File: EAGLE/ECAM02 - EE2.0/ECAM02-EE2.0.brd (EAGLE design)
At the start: 82.6 x 75.9 mm, 54 parts, among them J1 MODULAR TOOL, J2 SPI, J3 MOT, J4 FTDI, J5 S4B-PH-SM4, J6 S5B-PH-SM, J7 RINGLIGHT, Q2 16MHz, U1 SP3485, U10 MCP4725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

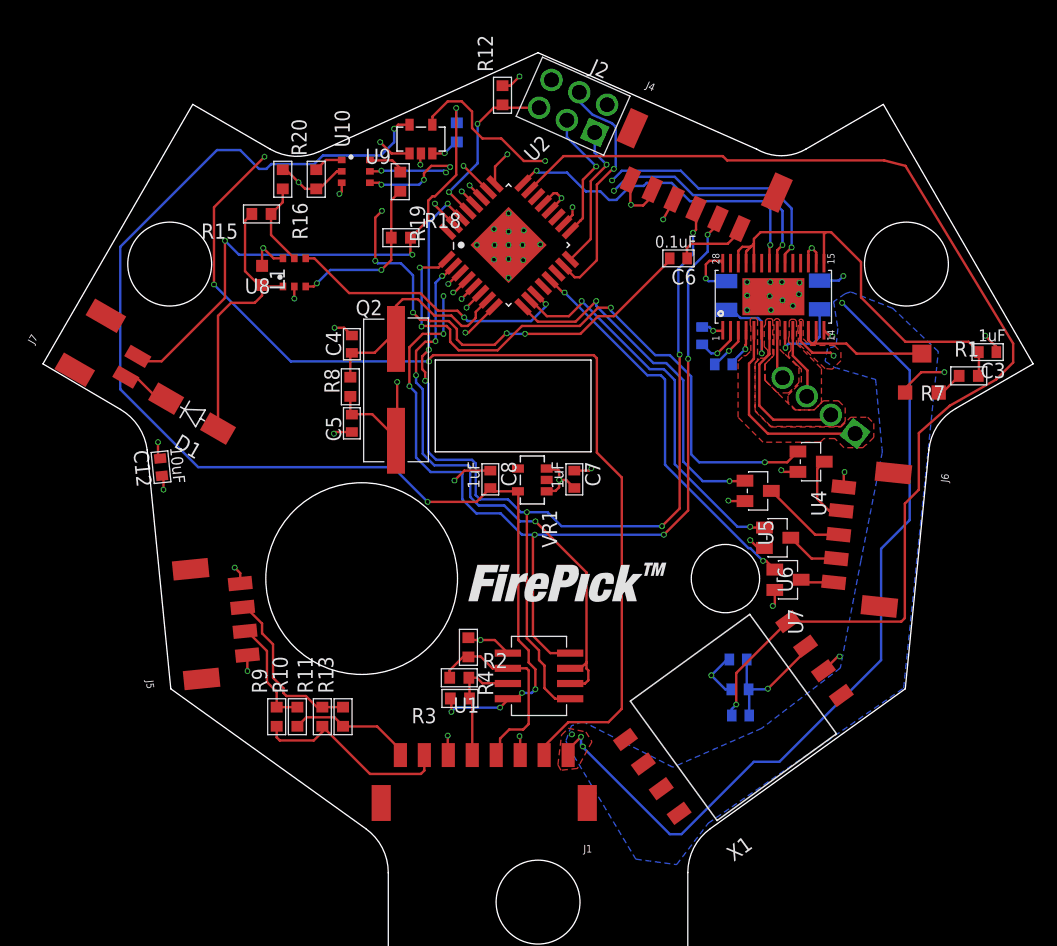
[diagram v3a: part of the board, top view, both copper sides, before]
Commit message: Completed boards. Please look at airwires connecting thermal pads to GND vias. They shouldn't be present due to the vias.
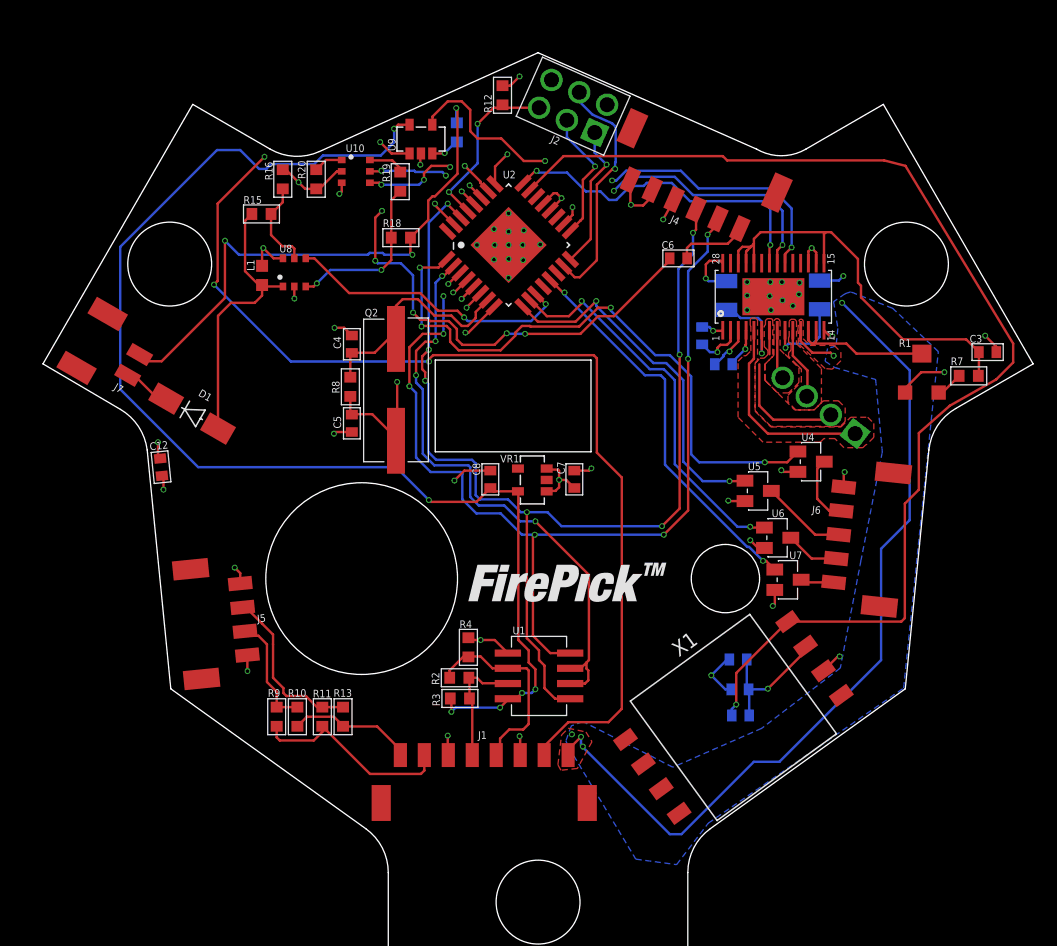
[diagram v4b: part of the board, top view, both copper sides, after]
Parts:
- moved J7 0.22 mm to (7.57, 49.8)
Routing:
- net +24V: track 87.1 -> 77.4 mm
- net AOUT2: track 13.3 -> 12.1 mm

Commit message: Updated all boards to include changes for production
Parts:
- added C13, C14, C15, C16: 0.1uF, TinWhiskers:C0603
- added C17: 100uF, TinWhiskers:C-SMD-6.3MM
- added C18: 10uF, TinWhiskers:C-SMD-6.3MM
- added U11: NTR4003NT3G, TinWhiskers:SOT-23-3
- J3: device TinWhiskers:CON-HDR-4POS-MALE -> TinWhiskers:CON-JST-PH-2.0MM-4P-THRU-VRT
- J4: device TinWhiskers:CON-JST-PH-2.00MM-6P-SMT-VRT -> TinWhiskers:CON-HDR-6POS-MALE
- J6: value S5B-PH-SM -> SOL+PUMP; device TinWhiskers:CON-JST-PH-2.0MM-5P-SMT-VRT -> TinWhiskers:CON-JST-PH-2.0MM-7P-SMT-VRT
- U2: device TinWhiskers:32-TQFN -> TinWhiskers:32-TQF(ATMEGA)
- moved J5 20.1 mm to (24.5, 47.1), turned to 270 degrees
- moved R8 9.78 mm to (15.9, 47.3)
- moved C4 9.78 mm to (16.0, 50.9)
- moved C5 9.78 mm to (16.0, 44.3)
- moved Q2 9.78 mm to (19.7, 47.1)
- moved R6 7.90 mm to (67.9, 48.4), flipped to the top, turned to 140 degrees
- moved J4 5.08 mm to (57.7, 66.3)
- moved U4 3.71 mm to (60.6, 40.5)
- moved R5 3.28 mm to (53.9, 56.5), flipped to the top, turned to 180 degrees
- moved U5 2.36 mm to (57.6, 38.2)
- moved J6 2.15 mm to (66.2, 33.5)
- moved C8 0.91 mm to (36.4, 40.3)
- moved R10 0.91 mm to (21.2, 19.6)
- moved R11 0.91 mm to (23.3, 19.6)
- moved R13 0.91 mm to (25.0, 19.6)
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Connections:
- new net N$12: J6.7, U11.3
- new net PUMP: U11.1, U2.32
- net +24V: now also C17.NEG, J6.1
- net +3V3: now also C14.2, C16.2
- net +5V: now also C13.2, C15.2, C18.NEG, J6.2; no longer J6.1
- net GND: now also C13.1, C14.1, C15.1, C16.1, C17.POS, C18.POS, U11.2; no longer U2.PAD
- net SOL1: now also J6.3; no longer J6.2
- net SOL2: now also J6.4; no longer J6.3
- net SOL3: now also J6.5; no longer J6.4
- net SOL4: now also J6.6; no longer J6.5
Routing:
- net PUMP: track 0.00 -> 53.5 mm, vias 0 -> 1
- net USB_D+: track 9.59 -> 38.7 mm
- net +3V3: track 106.0 -> 130.7 mm, vias 6 -> 7
- net VOUT: track 97.1 -> 118.8 mm
- net USB_D-: track 14.2 -> 35.5 mm
- net +5V: track 33.1 -> 50.5 mm
- net AOUT1: track 16.7 -> 0.00 mm
- net GND: track 67.5 -> 81.5 mm, vias 49 -> 40
- net AOUT2: track 12.1 -> 2.00 mm
- net XTAL2: track 27.9 -> 36.3 mm, vias 2 -> 3
- net XTAL1: track 19.0 -> 26.9 mm
- net GATE2: track 30.2 -> 37.5 mm
- net DI: track 91.5 -> 98.2 mm
- net N$16: track 6.11 -> 12.3 mm
- net RO: track 92.6 -> 98.5 mm
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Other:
- board text added: "FTDI"
- board text added: "MOD TOOL"
- board text added: "RINGLIGHT"
- board text added: "SOLENOIDS"
- board text added: "SPI"
- board text added: "USB CAM"

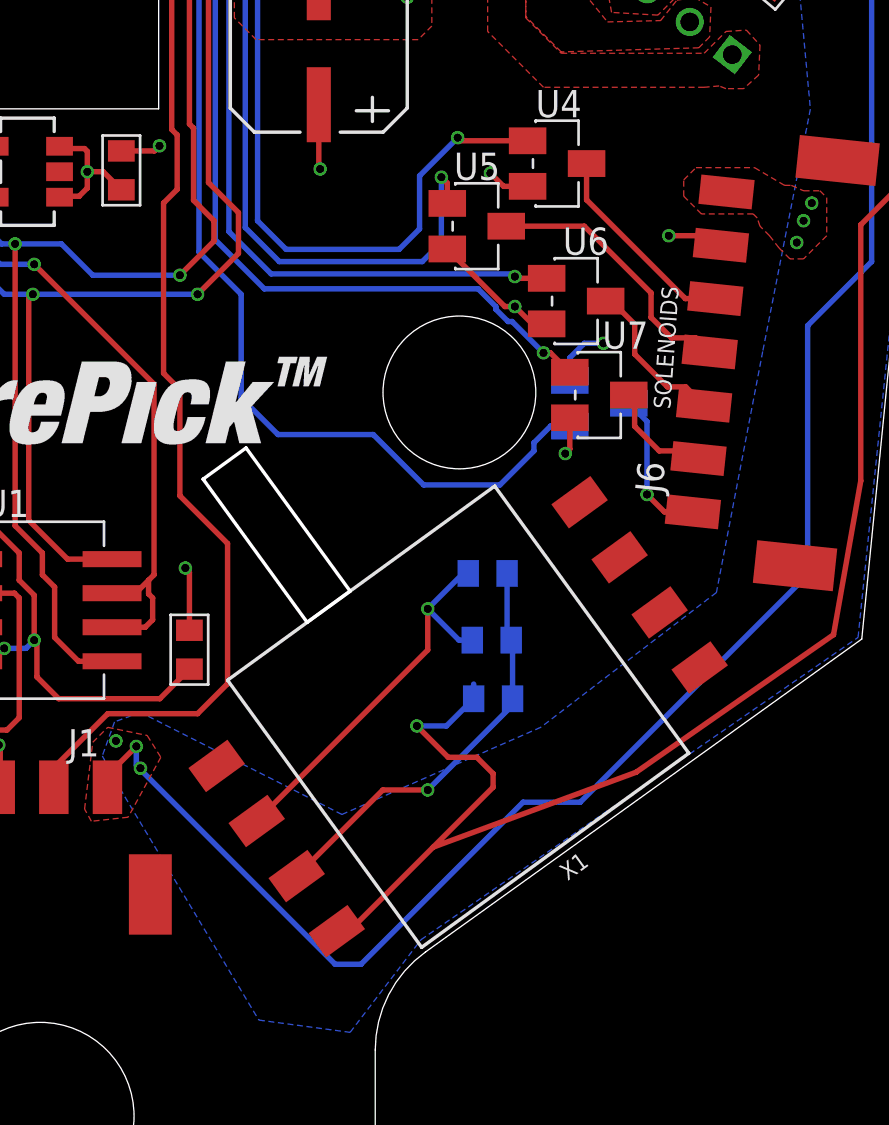
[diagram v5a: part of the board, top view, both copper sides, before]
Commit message: Updated motor hole size to 7mm Dia. Rerouted around.
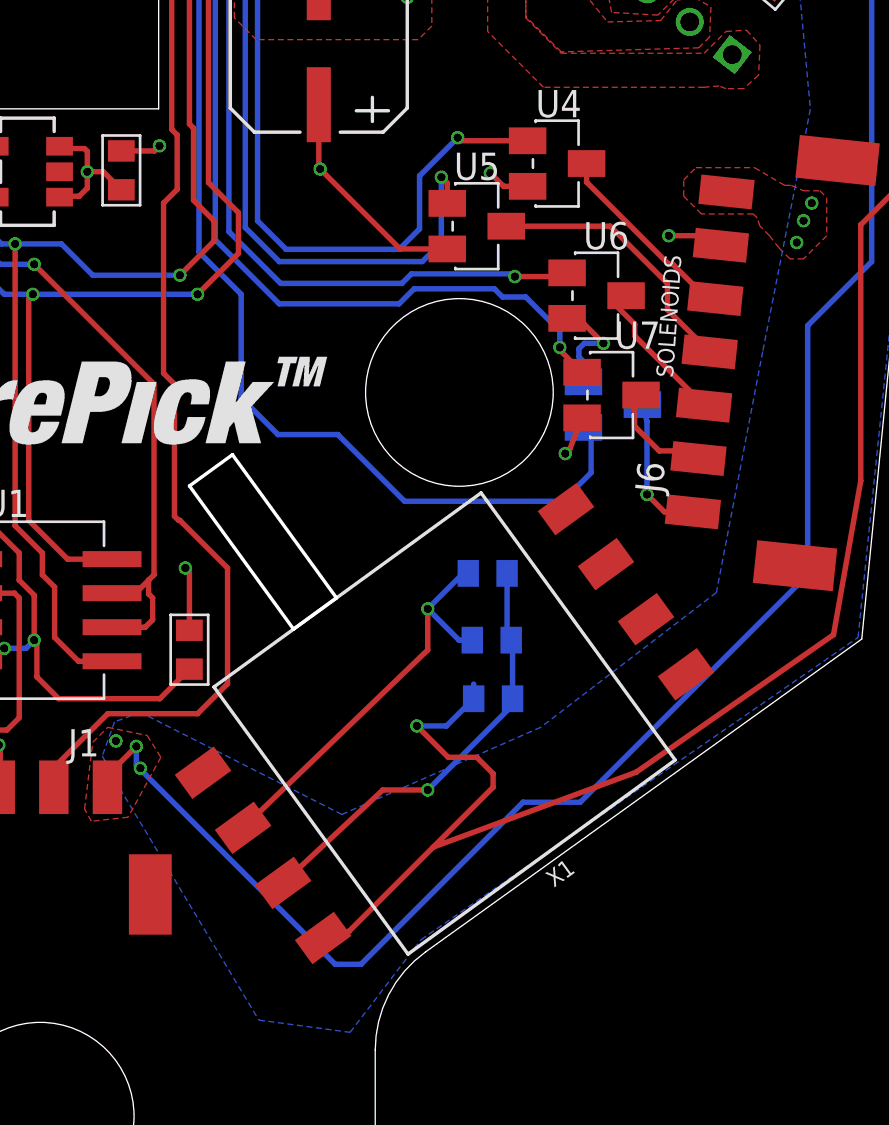
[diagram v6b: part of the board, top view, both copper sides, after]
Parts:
- moved U6 0.79 mm to (62.1, 35.6)
- moved X1 0.57 mm to (56.4, 19.6)
- moved U11 0.51 mm to (62.7, 31.5)
- moved U7 0.46 mm to (62.6, 31.9)
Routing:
- net GND: track 81.5 -> 84.9 mm, vias 40 -> 39
- net PUMP: track 53.5 -> 55.7 mm
- net GATE4: track 37.2 -> 38.5 mm
- net GATE3: track 36.9 -> 38.0 mm
- net SOL2: track 10.1 -> 10.8 mm
- net VOUT: track 118.8 -> 119.3 mm
- net +5V: track 50.5 -> 51.0 mm
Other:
- outline, holes or cut-outs redrawn

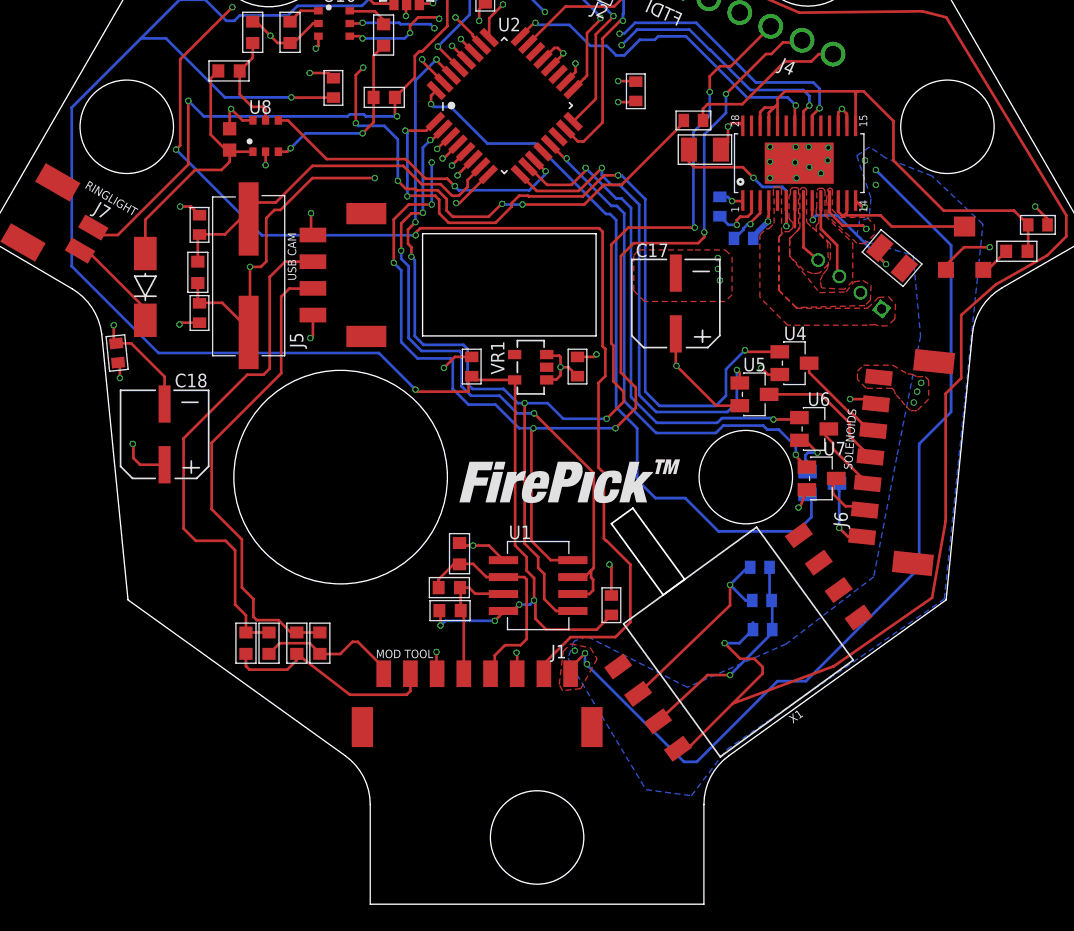
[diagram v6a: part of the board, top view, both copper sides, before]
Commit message: Partially-routed diff pairs
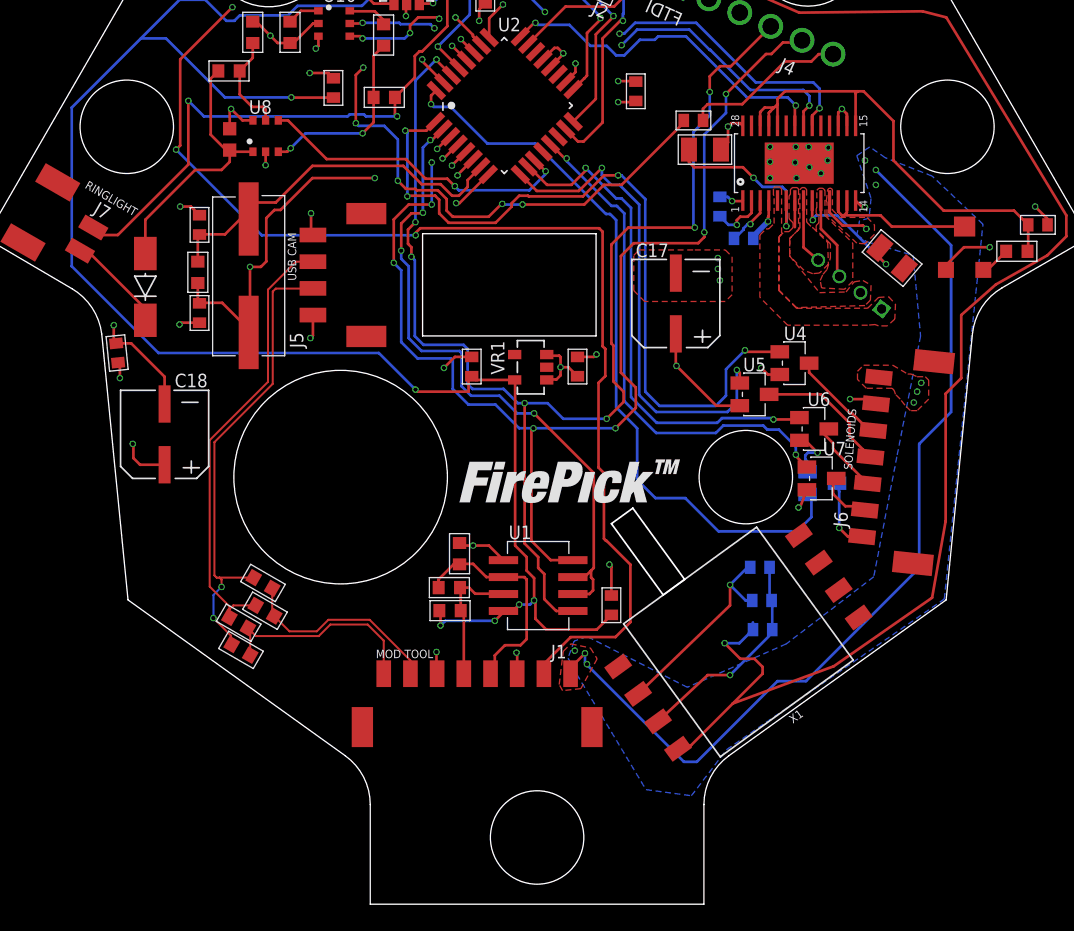
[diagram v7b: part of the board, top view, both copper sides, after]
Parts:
- moved R13 5.93 mm to (19.1, 19.1), turned to 150 degrees
- moved R11 5.18 mm to (20.8, 24.1), turned to 150 degrees
- moved R9 2.82 mm to (20.9, 22.0), turned to 150 degrees
- moved R10 2.74 mm to (19.0, 21.1), turned to 150 degrees
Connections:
- net EE_D+ renamed EE_P
- net EE_D- renamed EE_N
- net USB_D+ renamed USB_P
- net USB_D- renamed USB_N
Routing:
- net USB_P: track 38.7 -> 33.3 mm
- net EE_N: track 10.9 -> 15.9 mm
- net EE_P: track 16.6 -> 15.4 mm
- net USB_N: track 35.5 -> 35.1 mm, vias 0 -> 2
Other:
- board text added: "MILL"
- board text added: "MILL THIS AREA"

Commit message: Final(??) Versions of FPD boards.
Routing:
- net GND: track 84.9 -> 88.1 mm
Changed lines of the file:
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@@
 <wire x1="61.5872" y1="33.1548" x2="61.5872" y2="32.3968" width="0.2032" layer="16"/>
 <wire x1="60.6552" y1="55.5752" x2="60.96" y2="55.5244" width="0" layer="19" extent="1-1"/>
-<wire x1="68.838853125" y1="47.641053125" x2="71.9552" y2="47.5268" width="0" layer="19" extent="1-1"/>
+<wire x1="71.9552" y1="47.5268" x2="71.840946875" y2="47.641053125" width="0.2032" layer="1"/>
+<wire x1="71.840946875" y1="47.641053125" x2="68.838853125" y2="47.641053125" width="0.2032" layer="1"/>
 </signal>
 <signal name="+24V">
